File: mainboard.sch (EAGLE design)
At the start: 75 parts, among them Q3 MOSFET-PCHANNEL, Q4 MOSFET-PCHANNEL, T1 SINGLE_NCHAN_FET, T2 MOSFET_PCHAN_20A, T3 SINGLE_NCHAN_FET, T4 MOSFET_PCHAN_20A, T5 SINGLE_NCHAN_FET, T6 MOSFET_PCHAN_20A, U1 LT3688, U2 TEENSY_3.0+4, U3 RFM23BP, U4 HMC5883LSMD, U5 ITG-3200, U9 MIC803-31D3VM3TR

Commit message: Mainboard layout work
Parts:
- added R18, R19, R20: 4.7k, SparkFun-Resistors:RESISTOR0805-RES
- added R21, R23: 0R, SparkFun-Resistors:RESISTOR0805-RES
- added R22: 68k, SparkFun-Resistors:RESISTOR0805-RES
- added R24: 33k, SparkFun-Resistors:RESISTOR0805-RES
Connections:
- new net I2C_SCL: R18.1, U2.19/A5
- new net I2C_SDA: R19.1, U2.18/A4
- new net N$28: U3.SDO, U6.B1
- new net N$29: U3.SDI, U6.B2
- new net N$30: U3.SCK, U6.B3
- new net N$31: U3.NSEL, U6.B4
- new net N$32: R20.1, U2.0
- new net N$33: R21.2, U3.RXON
- new net N$34: R21.1, U3.GPIO_0
- new net N$35: R23.2, U3.TXON
- new net N$36: R23.1, U3.GPIO_1
- new net N$37: R22.1, R24.2, U2.14/A0
- new net RF_NIRQ: R20.2, U3.NIRQ
- new net SPI_MISO: U2.12, U6.A1
- new net SPI_MOSI: U2.11, U6.A2
- new net SPI_SCK: U2.13, U6.A3
- new net SPI_SS: U2.10, U6.A4
- net 3.3V: now also R18.2, R19.2
- net GND: now also R24.1, U3.SDN
- net I_SOLAR: now also U2.16/A2; no longer U2.14/A0
- net VBATT: now also R22.2
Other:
- moved on the sheet: Q3, Q4, R15, R16, R17, SMA1, U2, U4, U5, U6, U9

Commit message: More layout work on main board
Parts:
- added C14: 2.2nF, SparkFun-Capacitors:CAP0805
- added C15, C17, C18: 0.1uF, SparkFun-Capacitors:CAP0805
- added C16: 10nF, SparkFun-Capacitors:CAP0805
- added C19: 4.7uF, SparkFun-Capacitors:CAP0805
- added C20: .22uF, SparkFun-Capacitors:CAP0805
- added C21: 100uF, SparkFun-Capacitors:CAP1206
- added X1: CRYSTAL.ABS07, abracon:CRYSTAL.ABS07
- R18, R19: value 4.7k -> 2.2k
- U9: value MIC803-31D3VM3TR -> MIC803
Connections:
- new net N$38: U$1.XI, X1.1
- new net N$39: C14.1, U5.CPOUT
- new net N$40: C15.1, U5.REGOUT
- new net N$41: U$1.XO, X1.2
- new net N$42: C19.1, U4.C1
- new net N$43: C20.1, U4.SETP
- new net N$44: C20.2, U4.SETC
- net 3.3V: now also C16.1, C17.1, C18.1, U4.S1, U4.VDD, U4.VDDIO, U5.VDD, U5.VLOGIC
- net GND: now also C14.2, C15.2, C16.2, C17.2, C18.2, C19.2, C21.2, U4.GND@1, U4.GND@2, U5.AD0, U5.CLKIN, U5.GND, U5.RESV-G
- net I2C_SCL: now also U$1.SCL, U4.SCL, U5.SCL
- net I2C_SDA: now also U$1.SDA, U4.SDA, U5.SDA
- net VBACKUP: now also C21.1, U$1.VBAT
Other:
- moved on the sheet: U4, U5

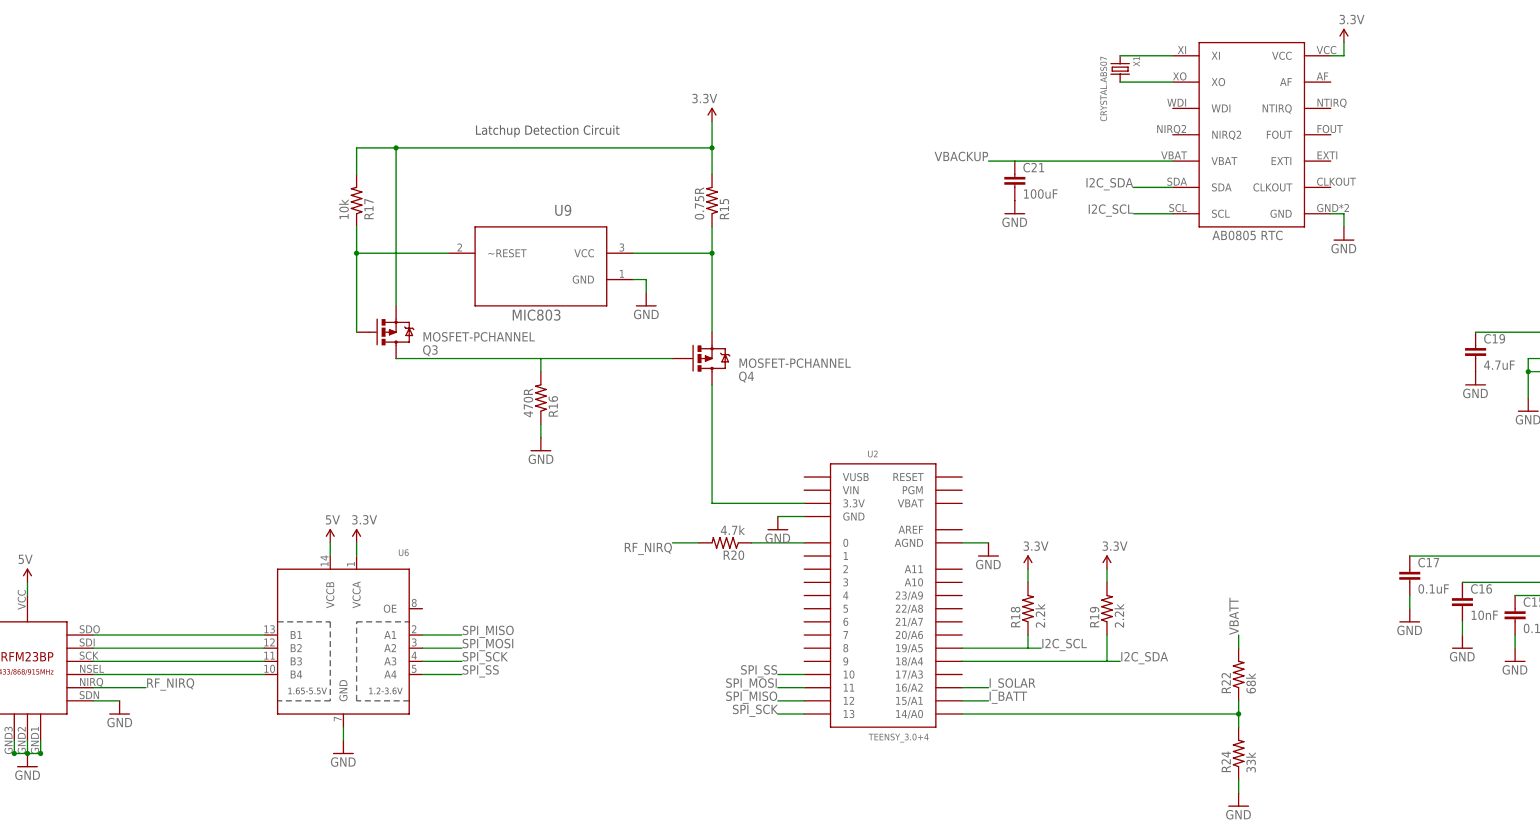
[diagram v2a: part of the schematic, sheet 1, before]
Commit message: Finished RTC schematic
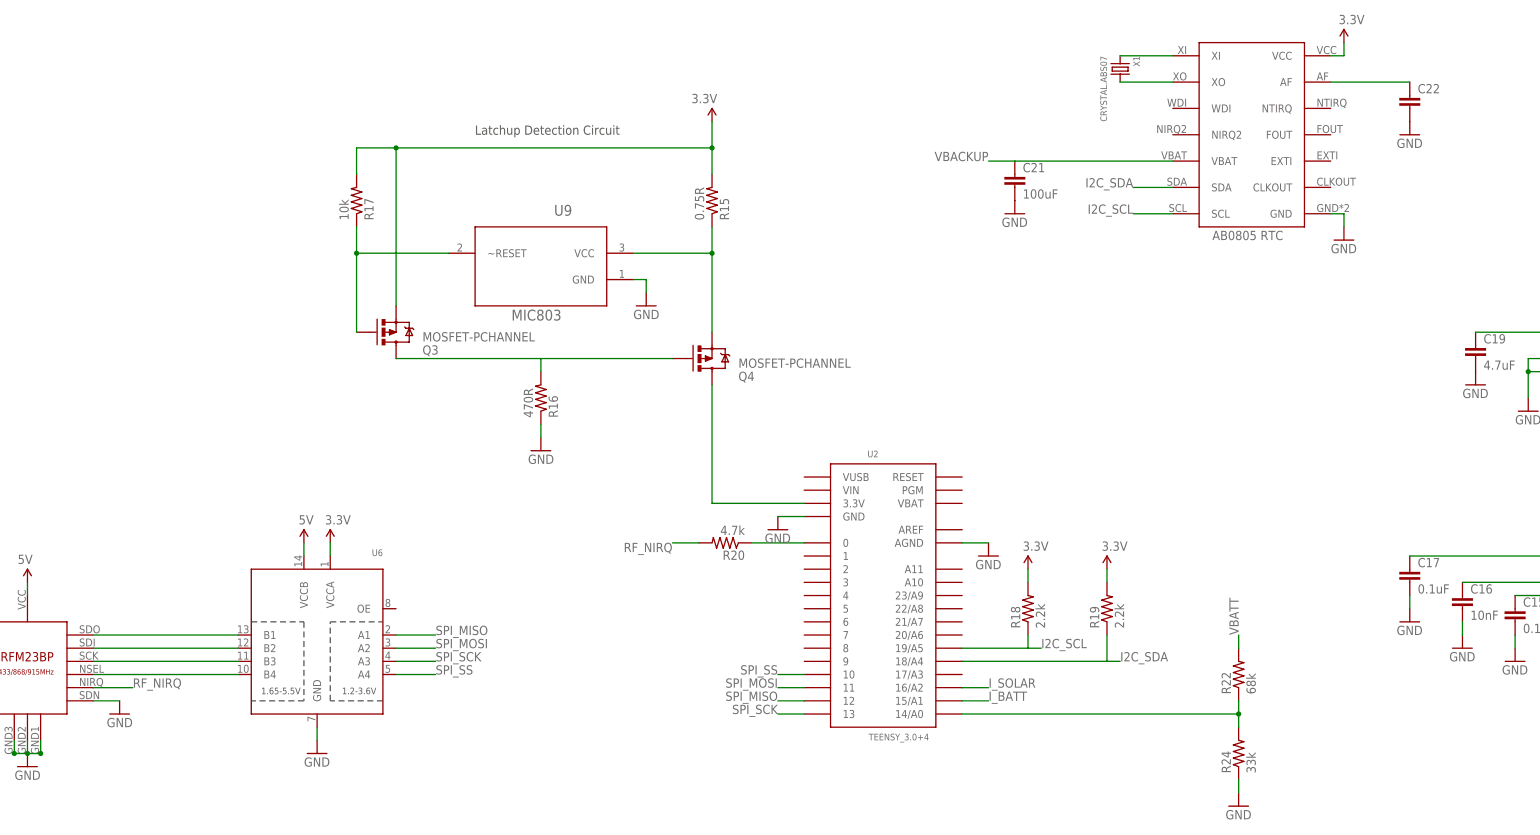
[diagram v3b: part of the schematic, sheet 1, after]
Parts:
- added C22: (no value), SparkFun-Capacitors:CAP0805
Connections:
- new net N$45: C22.1, U$1.AF
- net GND: now also C22.2
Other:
- moved on the sheet: U6
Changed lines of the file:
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@@
 <part name="GND39" library="SparkFun" deviceset="GND" device=""/>
 <part name="X1" library="abracon" deviceset="CRYSTAL" device=".ABS07"/>
+<part name="C22" library="SparkFun-Capacitors" deviceset="CAP" device="0805"/>
+<part name="GND40" library="SparkFun" deviceset="GND" device=""/>
 </parts>
 <sheets>
@@
 <instance part="U5" gate="G$1" x="226.06" y="-10.16"/>
 <instance part="U4" gate="G$1" x="208.28" y="43.18"/>
-<instance part="U6" gate="G$1" x="-38.1" y="-20.32" rot="MR0"/>
+<instance part="U6" gate="G$1" x="-43.18" y="-20.32" rot="MR0"/>
 <instance part="P+5" gate="G$1" x="33.02" y="81.28" rot="MR0"/>
 <instance part="SMA1" gate="G$1" x="-119.38" y="-40.64" rot="MR90"/>
@@
 <instance part="SUPPLY2" gate="G$1" x="-99.06" y="-7.62" rot="MR0"/>
 <instance part="GND12" gate="1" x="-99.06" y="-43.18" rot="MR0"/>
-<instance part="SUPPLY4" gate="G$1" x="-40.64" y="0"/>
-<instance part="P+3" gate="G$1" x="-35.56" y="0"/>
-<instance part="GND14" gate="1" x="-38.1" y="-40.64"/>
+<instance part="SUPPLY4" gate="G$1" x="-45.72" y="0"/>
+<instance part="P+3" gate="G$1" x="-40.64" y="0"/>
+<instance part="GND14" gate="1" x="-43.18" y="-40.64"/>
 <instance part="U$1" gate="G$1" x="137.16" y="78.74"/>
 <instance part="GND22" gate="1" x="154.94" y="58.42"/>
@@
 <instance part="GND39" gate="1" x="91.44" y="63.5"/>
 <instance part="X1" gate="G$1" x="111.76" y="91.44" rot="R270"/>
+<instance part="C22" gate="G$1" x="167.64" y="83.82"/>
+<instance part="GND40" gate="1" x="167.64" y="78.74"/>
 </instances>
 <busses>
@@
 <pinref part="GND14" gate="1" pin="GND"/>
 <pinref part="U6" gate="G$1" pin="GND"/>
-<wire x1="-38.1" y1="-38.1" x2="-38.1" y2="-35.56" width="0.1524" layer="91"/>
+<wire x1="-43.18" y1="-38.1" x2="-43.18" y2="-35.56" width="0.1524" layer="91"/>
 </segment>
 <segment>
@@
 <pinref part="GND39" gate="1" pin="GND"/>
 </segment>
+<segment>
+<pinref part="C22" gate="G$1" pin="2"/>
+<pinref part="GND40" gate="1" pin="GND"/>
+</segment>
 </net>
 <net name="3.3V" class="0">
@@
 <pinref part="P+3" gate="G$1" pin="3.3V"/>
 <pinref part="U6" gate="G$1" pin="VCCA"/>
-<wire x1="-35.56" y1="0" x2="-35.56" y2="-2.54" width="0.1524" layer="91"/>
+<wire x1="-40.64" y1="0" x2="-40.64" y2="-2.54" width="0.1524" layer="91"/>
 </segment>
 <segment>
@@
 <pinref part="U6" gate="G$1" pin="VCCB"/>
 <pinref part="SUPPLY4" gate="G$1" pin="5V"/>
-<wire x1="-40.64" y1="-2.54" x2="-40.64" y2="0" width="0.1524" layer="91"/>
+<wire x1="-45.72" y1="-2.54" x2="-45.72" y2="0" width="0.1524" layer="91"/>
 </segment>
 </net>
@@
 <segment>
 <pinref part="U6" gate="G$1" pin="A4"/>
-<wire x1="-22.86" y1="-25.4" x2="-15.24" y2="-25.4" width="0.1524" layer="91"/>
-<label x="-15.24" y="-25.4" size="1.778" layer="95"/>
+<wire x1="-27.94" y1="-25.4" x2="-20.32" y2="-25.4" width="0.1524" layer="91"/>
+<label x="-20.32" y="-25.4" size="1.778" layer="95"/>
 </segment>
 </net>
@@
 <segment>
 <pinref part="U6" gate="G$1" pin="A2"/>
-<wire x1="-22.86" y1="-20.32" x2="-15.24" y2="-20.32" width="0.1524" layer="91"/>
-<label x="-15.24" y="-20.32" size="1.778" layer="95"/>
+<wire x1="-27.94" y1="-20.32" x2="-20.32" y2="-20.32" width="0.1524" layer="91"/>
+<label x="-20.32" y="-20.32" size="1.778" layer="95"/>
 </segment>
 </net>
@@
 <segment>
 <pinref part="U6" gate="G$1" pin="A1"/>
-<wire x1="-22.86" y1="-17.78" x2="-15.24" y2="-17.78" width="0.1524" layer="91"/>
-<label x="-15.24" y="-17.78" size="1.778" layer="95"/>
+<wire x1="-27.94" y1="-17.78" x2="-20.32" y2="-17.78" width="0.1524" layer="91"/>
+<label x="-20.32" y="-17.78" size="1.778" layer="95"/>
 </segment>
 </net>
@@
 <segment>
 <pinref part="U6" gate="G$1" pin="A3"/>
-<wire x1="-22.86" y1="-22.86" x2="-15.24" y2="-22.86" width="0.1524" layer="91"/>
-<label x="-15.24" y="-22.86" size="1.778" layer="95"/>
+<wire x1="-27.94" y1="-22.86" x2="-20.32" y2="-22.86" width="0.1524" layer="91"/>
+<label x="-20.32" y="-22.86" size="1.778" layer="95"/>
 </segment>
 </net>
@@
 <pinref part="U3" gate="G$1" pin="SDO"/>
 <pinref part="U6" gate="G$1" pin="B1"/>
-<wire x1="-86.36" y1="-17.78" x2="-53.34" y2="-17.78" width="0.1524" layer="91"/>
+<wire x1="-86.36" y1="-17.78" x2="-58.42" y2="-17.78" width="0.1524" layer="91"/>
 </segment>
 </net>
@@
 <pinref part="U3" gate="G$1" pin="SDI"/>
 <pinref part="U6" gate="G$1" pin="B2"/>
-<wire x1="-86.36" y1="-20.32" x2="-53.34" y2="-20.32" width="0.1524" layer="91"/>
+<wire x1="-86.36" y1="-20.32" x2="-58.42" y2="-20.32" width="0.1524" layer="91"/>
 </segment>
 </net>
@@
 <pinref part="U3" gate="G$1" pin="SCK"/>
 <pinref part="U6" gate="G$1" pin="B3"/>
-<wire x1="-86.36" y1="-22.86" x2="-53.34" y2="-22.86" width="0.1524" layer="91"/>
+<wire x1="-86.36" y1="-22.86" x2="-58.42" y2="-22.86" width="0.1524" layer="91"/>
 </segment>
 </net>
@@
 <pinref part="U3" gate="G$1" pin="NSEL"/>
 <pinref part="U6" gate="G$1" pin="B4"/>
-<wire x1="-86.36" y1="-25.4" x2="-53.34" y2="-25.4" width="0.1524" layer="91"/>
+<wire x1="-86.36" y1="-25.4" x2="-58.42" y2="-25.4" width="0.1524" layer="91"/>
 </segment>
 </net>
@@
 <segment>
 <pinref part="U3" gate="G$1" pin="NIRQ"/>
-<wire x1="-86.36" y1="-27.94" x2="-76.2" y2="-27.94" width="0.1524" layer="91"/>
-<label x="-76.2" y="-27.94" size="1.778" layer="95"/>
+<wire x1="-86.36" y1="-27.94" x2="-78.74" y2="-27.94" width="0.1524" layer="91"/>
+<label x="-78.74" y="-27.94" size="1.778" layer="95"/>
 </segment>
 <segment>
@@
 </segment>
 </net>
+<net name="N$45" class="0">
+<segment>
+<pinref part="U$1" gate="G$1" pin="AF"/>
+<pinref part="C22" gate="G$1" pin="1"/>
+<wire x1="152.4" y1="88.9" x2="167.64" y2="88.9" width="0.1524" layer="91"/>
+</segment>
+</net>

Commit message: Got rid of level shifter for RF23BP
Looks like it’s not necessary after some experimentation
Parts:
- removed JP1, JP2, JP3, JP4, JP5: M025MM, SparkFun-Connectors:M025MM
- removed R20: 4.7k, SparkFun-Resistors:RESISTOR0805-RES
- removed U6: (no value), SparkFun-DigitalIC:TXB0104PWR
- added SP1, SP2, SP3, SP4, SP5: G125-FV20605L0P, G125-FV20605L0P:G125-FV20605L0P
- ST1, ST2, ST3, ST4, ST5: value G125-FV20605L0P -> M023.5MM_LOCK; device G125-FV20605L0P:G125-FV20605L0P -> SparkFun-Connectors:M023.5MM_LOCK
- renumbered ST6 to SP6
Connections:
- removed net N$28: U3.SDO, U6.B1
- removed net N$29: U3.SDI, U6.B2
- removed net N$30: U3.SCK, U6.B3
- removed net N$31: U3.NSEL, U6.B4
- removed net N$32: R20.1, U2.0
- new net RF_SDN: U2.1, U3.SDN
- new net UART_RX: U2.7
- new net UART_TX: U2.8
- net 3.3V: no longer U6.VCCA
- net 5V: no longer U6.VCCB
- net BATT_INPUT: now also ST1.2, ST2.2, ST3.2; no longer JP1.2, JP2.2, JP4.2
- net ENAB_BURN1: now also U2.2
- net ENAB_BURN2: now also U2.3
- net ENAB_BURN3: now also U2.4
- net GND: now also SP1.P1, SP1.P4, SP2.P1, SP2.P4, SP3.P1, SP3.P4, SP4.P1, SP4.P4, SP5.P1, SP5.P4, ST1.1, ST2.1, ST5.1; no longer JP1.1, JP2.1, JP3.1, ST1.P1, ST1.P4, ST2.P1, ST2.P4, ST3.P1, ST3.P4, ST4.P1, ST4.P4, ST5.P1, ST5.P4, U3.SDN, U6.GND
- net N$4: now also ST3.1, ST4.2; no longer JP4.1, JP5.2
- net RF_NIRQ: now also U2.0; no longer R20.2
- net SPI_MISO: now also U3.SDO; no longer U6.A1
- net SPI_MOSI: now also U3.SDI; no longer U6.A2
- net SPI_SCK: now also U3.SCK; no longer U6.A3
- net SPI_SS: now also U3.NSEL; no longer U6.A4
- net VBURN1: now also SP2.P2, SP2.P5; no longer ST2.P2, ST2.P5
- net VBURN2: now also SP4.P2, SP4.P5; no longer ST4.P2, ST4.P5
- net VBURN3: now also ST5.2; no longer JP3.2
- net VREG_IN: now also ST4.1; no longer JP5.1
- net VSOLAR: now also SP1.P3, SP1.P6, SP2.P3, SP2.P6, SP3.P3, SP3.P6, SP4.P3, SP4.P6, SP5.P3, SP5.P6; no longer ST1.P3, ST1.P6, ST2.P3, ST2.P6, ST3.P3, ST3.P6, ST4.P3, ST4.P6, ST5.P3, ST5.P6
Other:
- moved on the sheet: R19, R21, R23, SMA1

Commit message: Mainboard layout work
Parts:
- removed R21, R23: 0R, SparkFun-Resistors:RESISTOR0805-RES
- added C23: 0.1uF, SparkFun-Capacitors:CAP0805
- added R20, R25: 4R, SparkFun-Resistors:RESISTOR2512
- C22: value (none) -> 47pF
- R1, R4: device rcl:R-US_R1210 -> SparkFun-Resistors:RESISTOR2512
- R18, R19: value 2.2k -> 4.7k
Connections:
- removed net N$33: R21.2, U3.RXON
- removed net N$34: R21.1, U3.GPIO_0
- removed net N$35: R23.2, U3.TXON
- removed net N$36: R23.1, U3.GPIO_1
- new net VBURN_IN: R2.2, R20.1, R25.1, R27.2, R6.2, T2.S@1, T2.S@2, T2.S@3, T4.S@1, T4.S@2, T4.S@3, T6.S@1, T6.S@2, T6.S@3
- net 3.3V: now also C23.1
- net GND: now also C23.2
- net VREG_IN: now also R20.2, R25.2; no longer R2.2, R27.2, R6.2, T2.S@1, T2.S@2, T2.S@3, T4.S@1, T4.S@2, T4.S@3, T6.S@1, T6.S@2, T6.S@3
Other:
- moved on the sheet: C12, C22, R5

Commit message: More layout work
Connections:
- net VBURN1: now also SP4.P2, SP4.P5; no longer SP2.P2, SP2.P5
- net VBURN2: now also SP2.P2, SP2.P5; no longer SP4.P2, SP4.P5
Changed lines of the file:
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@@
 <grid distance="0.1" unitdist="inch" unit="inch" style="lines" multiple="1" display="no" altdistance="0.01" altunitdist="inch" altunit="inch"/>
 <layers>
-<layer number="1" name="Top" color="4" fill="1" visible="yes" active="no"/>
-<layer number="2" name="Route2" color="1" fill="3" visible="yes" active="no"/>
-<layer number="3" name="Route3" color="4" fill="3" visible="yes" active="no"/>
-<layer number="14" name="Route14" color="1" fill="6" visible="yes" active="no"/>
-<layer number="15" name="Route15" color="4" fill="6" visible="yes" active="no"/>
-<layer number="16" name="Bottom" color="1" fill="1" visible="yes" active="no"/>
-<layer number="17" name="Pads" color="2" fill="1" visible="yes" active="no"/>
-<layer number="18" name="Vias" color="2" fill="1" visible="yes" active="no"/>
-<layer number="19" name="Unrouted" color="6" fill="1" visible="yes" active="no"/>
-<layer number="20" name="Dimension" color="15" fill="1" visible="yes" active="no"/>
-<layer number="21" name="tPlace" color="7" fill="1" visible="yes" active="no"/>
-<layer number="22" name="bPlace" color="7" fill="1" visible="yes" active="no"/>
-<layer number="23" name="tOrigins" color="15" fill="1" visible="yes" active="no"/>
-<layer number="24" name="bOrigins" color="15" fill="1" visible="yes" active="no"/>
-<layer number="25" name="tNames" color="7" fill="1" visible="yes" active="no"/>
-<layer number="26" name="bNames" color="7" fill="1" visible="yes" active="no"/>
-<layer number="27" name="tValues" color="7" fill="1" visible="yes" active="no"/>
-<layer number="28" name="bValues" color="7" fill="1" visible="yes" active="no"/>
+<layer number="1" name="Top" color="4" fill="1" visible="no" active="no"/>
+<layer number="2" name="Route2" color="1" fill="3" visible="no" active="no"/>
+<layer number="3" name="Route3" color="4" fill="3" visible="no" active="no"/>
+<layer number="14" name="Route14" color="1" fill="6" visible="no" active="no"/>
+<layer number="15" name="Route15" color="4" fill="6" visible="no" active="no"/>
+<layer number="16" name="Bottom" color="1" fill="1" visible="no" active="no"/>
+<layer number="17" name="Pads" color="2" fill="1" visible="no" active="no"/>
+<layer number="18" name="Vias" color="2" fill="1" visible="no" active="no"/>
+<layer number="19" name="Unrouted" color="6" fill="1" visible="no" active="no"/>
+<layer number="20" name="Dimension" color="15" fill="1" visible="no" active="no"/>
+<layer number="21" name="tPlace" color="7" fill="1" visible="no" active="no"/>
+<layer number="22" name="bPlace" color="7" fill="1" visible="no" active="no"/>
+<layer number="23" name="tOrigins" color="15" fill="1" visible="no" active="no"/>
+<layer number="24" name="bOrigins" color="15" fill="1" visible="no" active="no"/>
+<layer number="25" name="tNames" color="7" fill="1" visible="no" active="no"/>
+<layer number="26" name="bNames" color="7" fill="1" visible="no" active="no"/>
+<layer number="27" name="tValues" color="7" fill="1" visible="no" active="no"/>
+<layer number="28" name="bValues" color="7" fill="1" visible="no" active="no"/>
 <layer number="29" name="tStop" color="7" fill="3" visible="no" active="no"/>
 <layer number="30" name="bStop" color="7" fill="6" visible="no" active="no"/>
@@
 <layer number="35" name="tGlue" color="7" fill="4" visible="no" active="no"/>
 <layer number="36" name="bGlue" color="7" fill="5" visible="no" active="no"/>
-<layer number="37" name="tTest" color="7" fill="1" visible="yes" active="no"/>
-<layer number="38" name="bTest" color="7" fill="1" visible="yes" active="no"/>
+<layer number="37" name="tTest" color="7" fill="1" visible="no" active="no"/>
+<layer number="38" name="bTest" color="7" fill="1" visible="no" active="no"/>
 <layer number="39" name="tKeepout" color="4" fill="11" visible="no" active="no"/>
 <layer number="40" name="bKeepout" color="1" fill="11" visible="no" active="no"/>
@@
 <layer number="44" name="Drills" color="7" fill="1" visible="no" active="no"/>
 <layer number="45" name="Holes" color="7" fill="1" visible="no" active="no"/>
-<layer number="46" name="Milling" color="3" fill="1" visible="yes" active="no"/>
-<layer number="47" name="Measures" color="7" fill="1" visible="yes" active="no"/>
-<layer number="48" name="Document" color="7" fill="1" visible="yes" active="no"/>
-<layer number="49" name="Reference" color="7" fill="1" visible="yes" active="no"/>
-<layer number="50" name="dxf" color="7" fill="1" visible="yes" active="no"/>
-<layer number="51" name="tDocu" color="7" fill="1" visible="yes" active="no"/>
-<layer number="52" name="bDocu" color="7" fill="1" visible="yes" active="no"/>
-<layer number="53" name="tGND_GNDA" color="7" fill="9" visible="yes" active="no"/>
-<layer number="54" name="bGND_GNDA" color="1" fill="9" visible="yes" active="no"/>
-<layer number="56" name="wert" color="7" fill="1" visible="yes" active="no"/>
-<layer number="57" name="tCAD" color="7" fill="1" visible="yes" active="no"/>
+<layer number="46" name="Milling" color="3" fill="1" visible="no" active="no"/>
+<layer number="47" name="Measures" color="7" fill="1" visible="no" active="no"/>
+<layer number="48" name="Document" color="7" fill="1" visible="no" active="no"/>
+<layer number="49" name="Reference" color="7" fill="1" visible="no" active="no"/>
+<layer number="50" name="dxf" color="7" fill="1" visible="no" active="no"/>
+<layer number="51" name="tDocu" color="7" fill="1" visible="no" active="no"/>
+<layer number="52" name="bDocu" color="7" fill="1" visible="no" active="no"/>
+<layer number="53" name="tGND_GNDA" color="7" fill="9" visible="no" active="no"/>
+<layer number="54" name="bGND_GNDA" color="1" fill="9" visible="no" active="no"/>
+<layer number="56" name="wert" color="7" fill="1" visible="no" active="no"/>
+<layer number="57" name="tCAD" color="7" fill="1" visible="no" active="no"/>
 <layer number="91" name="Nets" color="2" fill="1" visible="yes" active="yes"/>
 <layer number="92" name="Busses" color="1" fill="1" visible="yes" active="yes"/>
@@
 </segment>
 </net>
-<net name="VBURN1" class="0">
+<net name="VBURN2" class="0">
+<segment>
+<pinref part="SP2" gate="G$1" pin="P5"/>
+<wire x1="-99.06" y1="88.9" x2="-93.98" y2="88.9" width="0.1524" layer="91"/>
+<label x="-93.98" y="88.9" size="1.778" layer="95"/>
+</segment>
 <segment>
 <pinref part="SP2" gate="G$1" pin="P2"/>
@@
 <label x="-129.54" y="88.9" size="1.778" layer="95" rot="MR0"/>
 </segment>
-<segment>
-<pinref part="SP2" gate="G$1" pin="P5"/>
-<wire x1="-99.06" y1="88.9" x2="-93.98" y2="88.9" width="0.1524" layer="91"/>
-<label x="-93.98" y="88.9" size="1.778" layer="95"/>
-</segment>
-</net>
-<net name="VBURN2" class="0">
+</net>
+<net name="VBURN1" class="0">
 <segment>
 <pinref part="SP4" gate="G$1" pin="P5"/>
